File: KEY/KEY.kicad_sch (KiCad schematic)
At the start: 41 parts, among them J1 BUS, J2 BATT_EXT, J3 FLASH/CONF, J4 TESLA TS25001, J5 KEYB, J6 RFID, Q1 BC846, Q2 BC846, Q3 BC857, SW1 tamper switch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

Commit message: Add pcb design
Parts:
- added TP3: TestPoint, TestPoint:TestPoint_Pad_1.5x1.5mm, symbol Connector:TestPoint
- J5: footprint (none) -> Connector_PinSocket_2.54mm:PinSocket_1x07_P2.54mm_Horizontal
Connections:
- net GND: now also TP3.1
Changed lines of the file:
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@@
+    )
+  )
+  (symbol (lib_name "GND_3") (lib_id "power:GND") (at 194.31 91.44 0) (unit 1)
+    (in_bom yes) (on_board yes) (dnp no) (fields_autoplaced)
+    (property "Reference" "#PWR023" (at 194.31 97.79 0)
+      (effects (font (size 1.27 1.27)) hide)
+    )
+    (property "Value" "GND" (at 194.31 96.52 0)
+      (effects (font (size 1.27 1.27)))
+    )
+    (property "Footprint" "" (at 194.31 91.44 0)
+      (effects (font (size 1.27 1.27)) hide)
+    )
+    (property "Datasheet" "" (at 194.31 91.44 0)
+      (effects (font (size 1.27 1.27)) hide)
+    )
+    (pin "1")
+    (instances
+      (project "KEY"
+        (path "/bd84660b-13bb-4554-9f23-8e30376967c6"
+          (reference "#PWR023") (unit 1)
+        )
+      )
     )
   )
@@
         (path "/bd84660b-13bb-4554-9f23-8e30376967c6"
           (reference "C5") (unit 1)
+        )
+      )
+    )
+  )
+  (symbol (lib_id "Connector:TestPoint") (at 194.31 91.44 0) (unit 1)
+    (in_bom yes) (on_board yes) (dnp no) (fields_autoplaced)
+    (property "Reference" "TP3" (at 196.85 86.868 0)
+      (effects (font (size 1.27 1.27)) (justify left))
+    )
+    (property "Value" "TestPoint" (at 196.85 89.408 0)
+      (effects (font (size 1.27 1.27)) (justify left))
+    )
+    (property "Footprint" "TestPoint:TestPoint_Pad_1.5x1.5mm" (at 199.39 91.44 0)
+      (effects (font (size 1.27 1.27)) hide)
+    )
+    (property "Datasheet" "~" (at 199.39 91.44 0)
+      (effects (font (size 1.27 1.27)) hide)
+    )
+    (pin "1")
+    (instances
+      (project "KEY"
+        (path "/bd84660b-13bb-4554-9f23-8e30376967c6"
+          (reference "TP3") (unit 1)
         )
       )
@@
       (effects (font (size 1.27 1.27)) (justify left))
     )
-    (property "Footprint" "" (at 100.33 142.24 0)
-      (effects (font (size 1.27 1.27)) hide)
-    )
+    (property "Footprint" "Connector_PinSocket_2.54mm:PinSocket_1x07_P2.54mm_Horizontal" (at 100.33 142.24 0)
+      (effects (font (size 1.27 1.27)) hide)
+    )

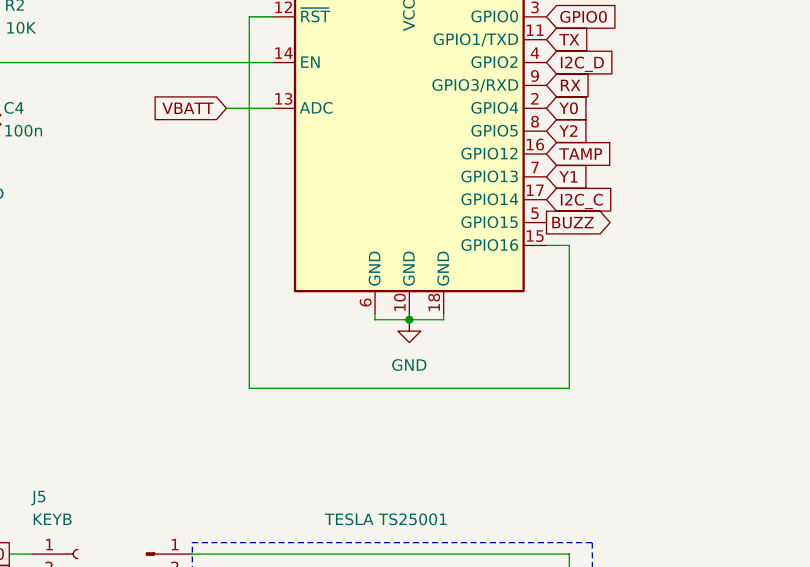
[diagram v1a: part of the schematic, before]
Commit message: Update symbol and footprint of WT8266
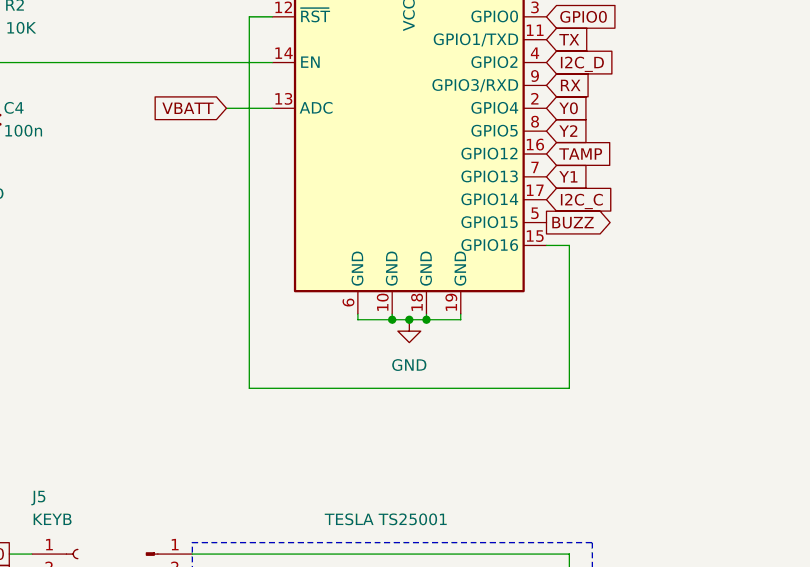
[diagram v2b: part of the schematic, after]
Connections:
- net GND: now also U2.19 (GND)
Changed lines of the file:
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@@
   (junction (at 42.545 31.75) (diameter 0) (color 0 0 0 0)
   )
+  (junction (at 139.065 108.585) (diameter 0) (color 0 0 0 0)
+  )
   (junction (at 252.73 93.98) (diameter 0) (color 0 0 0 0)
   )
@@
   (junction (at 154.94 158.75) (diameter 0) (color 0 0 0 0)
   )
+  (junction (at 135.255 108.585) (diameter 0) (color 0 0 0 0)
+  )
   (junction (at 54.61 41.91) (diameter 0) (color 0 0 0 0)
   )
@@
     (stroke (width 0) (type default))
   )
-  (wire (pts (xy 137.16 107.95) (xy 137.16 108.585))
-    (stroke (width 0) (type default))
-  )
   (wire (pts (xy 44.45 36.83) (xy 42.545 36.83))
     (stroke (width 0) (type default))
@@
     (stroke (width 0) (type default))
   )
-  (wire (pts (xy 133.35 108.585) (xy 137.16 108.585))
+  (wire (pts (xy 131.445 108.585) (xy 135.255 108.585))
     (stroke (width 0) (type default))
   )
@@
     (stroke (width 0) (type default))
   )
+  (wire (pts (xy 139.065 107.95) (xy 139.065 108.585))
+    (stroke (width 0) (type default))
+  )
   (wire (pts (xy 261.62 71.12) (xy 260.35 71.12))
     (stroke (width 0) (type default))
@@
     (stroke (width 0) (type default))
   )
+  (wire (pts (xy 135.255 107.95) (xy 135.255 108.585))
+    (stroke (width 0) (type default))
+  )
   (wire (pts (xy 154.94 134.62) (xy 154.94 148.59))
     (stroke (width 0) (type default))
@@
     (stroke (width 0) (type default))
   )
+  (wire (pts (xy 131.445 108.585) (xy 131.445 107.95))
+    (stroke (width 0) (type default))
+  )
   (wire (pts (xy 64.77 34.29) (xy 72.39 34.29))
     (stroke (width 0) (type default))
@@
     (stroke (width 0) (type default))
   )
+  (wire (pts (xy 142.875 108.585) (xy 142.875 107.95))
+    (stroke (width 0) (type default))
+  )
   (wire (pts (xy 125.73 162.56) (xy 125.73 163.83))
     (stroke (width 0) (type default))
@@
     (stroke (width 0) (type default))
   )
+  (wire (pts (xy 139.065 108.585) (xy 142.875 108.585))
+    (stroke (width 0) (type default))
+  )
   (wire (pts (xy 90.17 149.86) (xy 90.17 144.78))
     (stroke (width 0) (type default))
   )
-  (wire (pts (xy 137.16 108.585) (xy 140.97 108.585))
+  (wire (pts (xy 137.16 108.585) (xy 139.065 108.585))
     (stroke (width 0) (type default))
   )
@@
     (stroke (width 0) (type default))
   )
-  (wire (pts (xy 140.97 107.95) (xy 140.97 108.585))
-    (stroke (width 0) (type default))
-  )
   (wire (pts (xy 154.94 134.62) (xy 113.03 134.62))
     (stroke (width 0) (type default))
@@
     (stroke (width 0) (type default))
   )
-  (wire (pts (xy 133.35 107.95) (xy 133.35 108.585))
-    (stroke (width 0) (type default))
-  )
   (wire (pts (xy 260.35 59.69) (xy 260.35 60.96))
     (stroke (width 0) (type default))
@@
   )
   (wire (pts (xy 132.08 139.7) (xy 132.08 148.59))
+    (stroke (width 0) (type default))
+  )
+  (wire (pts (xy 135.255 108.585) (xy 137.16 108.585))
     (stroke (width 0) (type default))
   )
@@
       (effects (font (size 1.27 1.27)) hide)
     )
-    (property "Datasheet" "https://botland.cz/index.php?controller=attachment&id_attachment=1796" (at 128.27 87.63 0)
+    (property "Datasheet" "https://web.archive.org/web/20230921181528id_/http://ttcnc.co.kr/wp-content/uploads/2021/05/WT8266-S1-DataSheet-V2.5.pdf" (at 128.27 87.63 0)
       (effects (font (size 1.27 1.27)) hide)
     )
@@
     (pin "17")
     (pin "18")
+    (pin "19")
     (pin "2")
     (pin "3")
